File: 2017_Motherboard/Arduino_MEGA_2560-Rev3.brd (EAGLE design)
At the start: 100 x 80 mm, 77 parts, among them IC1 NCP1117ST50T3G, IC2 FT232RL, IC3 ATMEGA2560-16AU, IC7 LMV358IDGKR, X1 POWERSUPPLY_DC21MMX, Y1 CSTCE16M0V53-R0 16MHZ

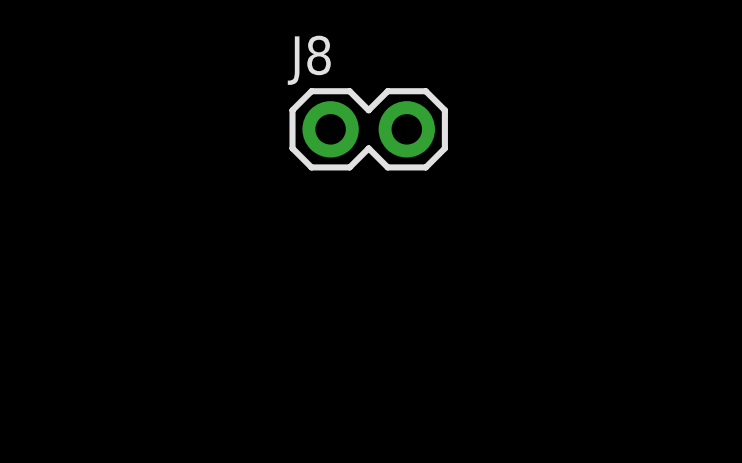
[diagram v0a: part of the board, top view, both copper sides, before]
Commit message: Added GND for PWMs
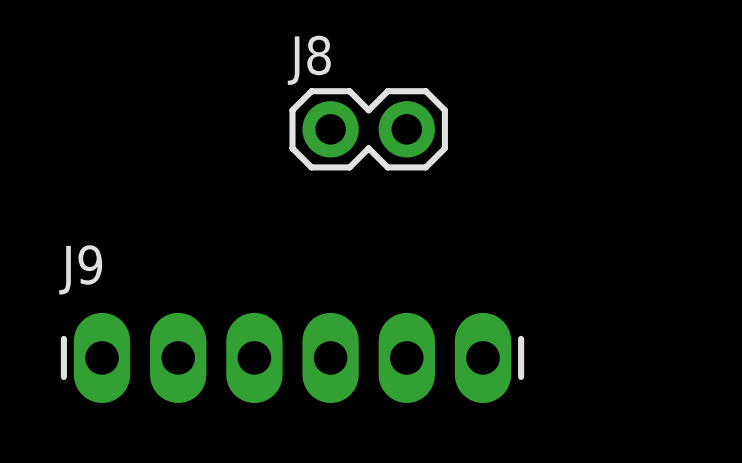
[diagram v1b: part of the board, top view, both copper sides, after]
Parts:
- added J9: (no value), SparkFun-Connectors:1X06_LONGPADS
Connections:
- net GND: now also J9.1, J9.2, J9.3, J9.4, J9.5, J9.6
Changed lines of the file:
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@@
 <?xml version="1.0" encoding="utf-8"?>
 <!DOCTYPE eagle SYSTEM "eagle.dtd">
-<eagle version="7.7.0">
+<eagle version="7.6.0">
 <drawing>
 <settings>
@@
 <element name="J7" library="SparkFun-Connectors" package="1X02" value="" x="-7.62" y="-266.7"/>
 <element name="J8" library="SparkFun-Connectors" package="1X02" value="" x="-7.62" y="-287.02"/>
+<element name="J9" library="SparkFun-Connectors" package="1X06_LONGPADS" value="" x="-15.24" y="-294.64"/>
 </elements>
 <signals>
@@
 <contactref element="J2" pad="4"/>
 <contactref element="J2" pad="3"/>
+<contactref element="J9" pad="6"/>
+<contactref element="J9" pad="5"/>
+<contactref element="J9" pad="4"/>
+<contactref element="J9" pad="3"/>
+<contactref element="J9" pad="2"/>
+<contactref element="J9" pad="1"/>
 <wire x1="-16.09" y1="-223.52" x2="-16.09" y2="-233.68" width="0" layer="19" extent="1-1"/>
 <wire x1="-8.47" y1="-223.52" x2="-16.09" y2="-223.52" width="0" layer="19" extent="1-1"/>
@@
 <wire x1="-16.09" y1="-86.36" x2="-16.09" y2="-91.44" width="0" layer="19" extent="1-1"/>
 <wire x1="-16.09" y1="-81.28" x2="-16.09" y2="-86.36" width="0" layer="19" extent="1-1"/>
+<wire x1="-15.24" y1="-294.64" x2="-16.09" y2="-233.68" width="0" layer="19" extent="1-1"/>
+<wire x1="-12.7" y1="-294.64" x2="-15.24" y2="-294.64" width="0" layer="19" extent="1-1"/>
+<wire x1="-10.16" y1="-294.64" x2="-12.7" y2="-294.64" width="0" layer="19" extent="1-1"/>
+<wire x1="-7.62" y1="-294.64" x2="-10.16" y2="-294.64" width="0" layer="19" extent="1-1"/>
+<wire x1="-5.08" y1="-294.64" x2="-7.62" y2="-294.64" width="0" layer="19" extent="1-1"/>
+<wire x1="-2.54" y1="-294.64" x2="-5.08" y2="-294.64" width="0" layer="19" extent="1-1"/>
 <wire x1="22.82" y1="2.46" x2="-16.09" y2="-81.28" width="0" layer="19" extent="1-1"/>
 <wire x1="25.36" y1="2.46" x2="22.82" y2="2.46" width="0" layer="19" extent="1-1"/>

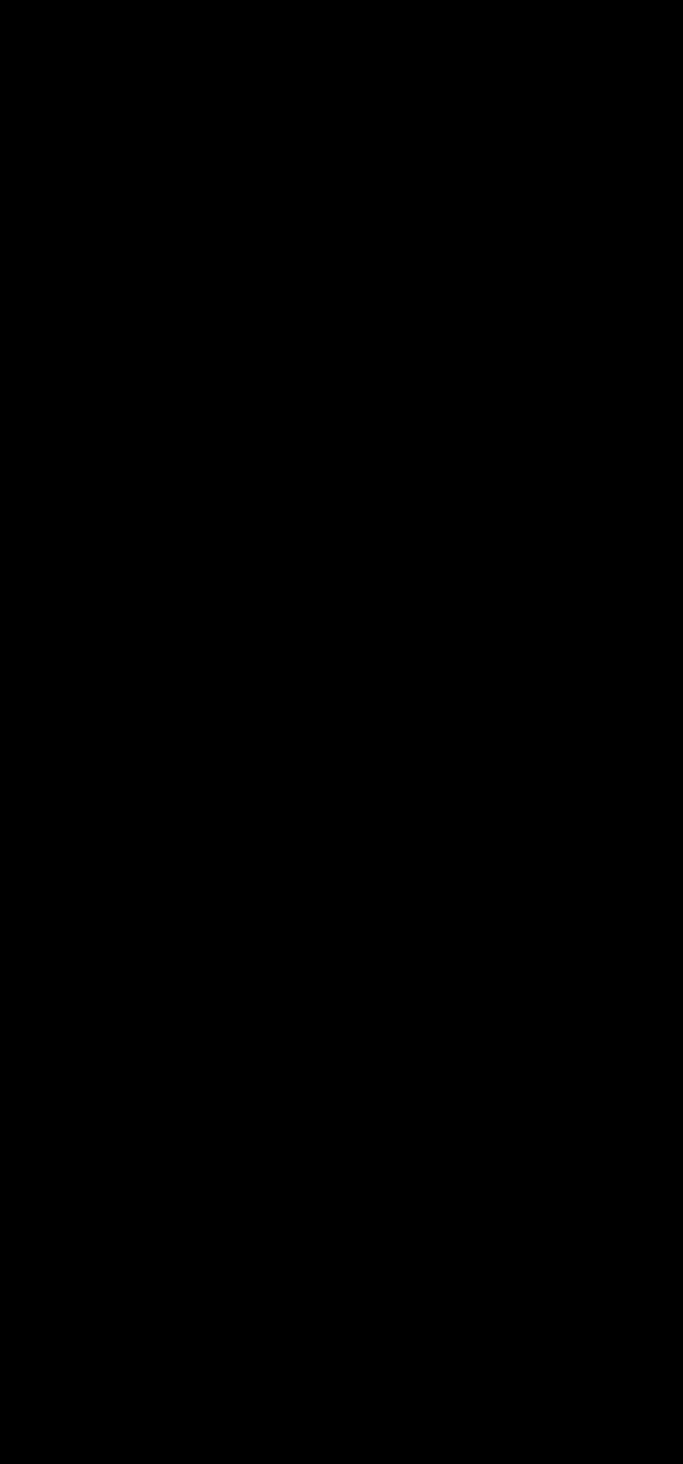
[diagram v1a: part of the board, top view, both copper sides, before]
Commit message: SchematicRev1
finished the schematic (hopefully), now we will work on the layout
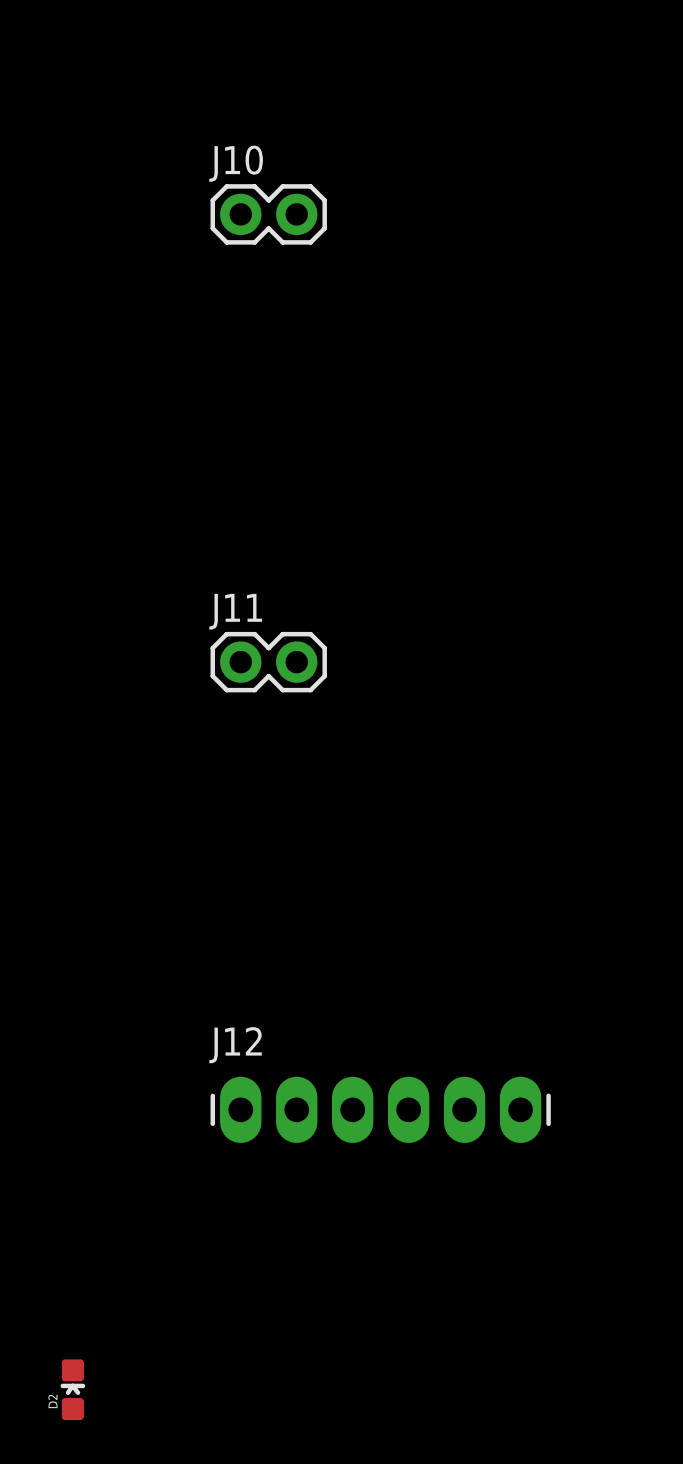
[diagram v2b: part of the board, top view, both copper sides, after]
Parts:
- added D2: RED, SparkFun-LED:LED-0603
- added J10, J11: (no value), SparkFun-Connectors:1X02
- added J12: (no value), SparkFun-Connectors:1X06_LONGPADS
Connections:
- new net N$15: D2.C, J11.2
- net +3V3: now also J10.1
- net +5V: now also J11.1, J12.2
- net FTDI_3.3V: now also J10.2
- net GND: now also J12.3
- net PA1: now also J12.6
- net PA2: now also J12.1
- net RXD1: now also J12.4
- net TXD1: now also J12.5
- net V_USB: now also D2.A
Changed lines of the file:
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@@
 <?xml version="1.0" encoding="utf-8"?>
 <!DOCTYPE eagle SYSTEM "eagle.dtd">
-<eagle version="7.6.0">
+<eagle version="7.7.0">
 <drawing>
 <settings>
@@
 <element name="J8" library="SparkFun-Connectors" package="1X02" value="" x="-7.62" y="-287.02"/>
 <element name="J9" library="SparkFun-Connectors" package="1X06_LONGPADS" value="" x="-15.24" y="-294.64"/>
+<element name="J10" library="SparkFun-Connectors" package="1X02" value="" x="-15.24" y="-314.96"/>
+<element name="J11" library="SparkFun-Connectors" package="1X02" value="" x="-15.24" y="-335.28"/>
+<element name="J12" library="SparkFun-Connectors" package="1X06_LONGPADS" value="" x="-15.24" y="-355.6"/>
+<element name="D2" library="SparkFun-LED" package="LED-0603" value="RED" x="-22.86" y="-368.3">
+<attribute name="PROD_ID" value="DIO-00819" x="-22.86" y="-368.3" size="1.778" layer="27" display="off"/>
+</element>
 </elements>
 <signals>
@@
 <contactref element="POWER" pad="5"/>
 <contactref element="POWER" pad="2"/>
+<contactref element="J11" pad="1"/>
+<contactref element="J12" pad="2"/>
 <wire x1="84.32" y1="67.43" x2="84.32" y2="68.23" width="0" layer="19" extent="1-1"/>
 <wire x1="84.98" y1="61.8" x2="84.32" y2="67.43" width="0" layer="19" extent="1-1"/>
@@
 <wire x1="18.74" y1="23.31" x2="16.7348" y2="12.78" width="0" layer="19" extent="1-1"/>
 <wire x1="36.265" y1="51.57" x2="54.8" y2="44.3464" width="0" layer="19" extent="1-1"/>
+<wire x1="-15.24" y1="-335.28" x2="27.9" y2="2.46" width="0" layer="19" extent="1-1"/>
+<wire x1="-12.7" y1="-355.6" x2="-15.24" y2="-335.28" width="0" layer="19" extent="1-1"/>
 </signal>
 <signal name="GND" class="2">
@@
 <contactref element="J9" pad="2"/>
 <contactref element="J9" pad="1"/>
+<contactref element="J12" pad="3"/>
 <wire x1="-16.09" y1="-223.52" x2="-16.09" y2="-233.68" width="0" layer="19" extent="1-1"/>
 <wire x1="-8.47" y1="-223.52" x2="-16.09" y2="-223.52" width="0" layer="19" extent="1-1"/>
@@
 <wire x1="-5.08" y1="-294.64" x2="-7.62" y2="-294.64" width="0" layer="19" extent="1-1"/>
 <wire x1="-2.54" y1="-294.64" x2="-5.08" y2="-294.64" width="0" layer="19" extent="1-1"/>
+<wire x1="-10.16" y1="-355.6" x2="-10.16" y2="-294.64" width="0" layer="19" extent="1-1"/>
 <wire x1="22.82" y1="2.46" x2="-16.09" y2="-81.28" width="0" layer="19" extent="1-1"/>
 <wire x1="25.36" y1="2.46" x2="22.82" y2="2.46" width="0" layer="19" extent="1-1"/>
@@
 <contactref element="POWER" pad="4"/>
 <contactref element="J8" pad="1"/>
+<contactref element="J10" pad="1"/>
+<wire x1="-7.62" y1="-287.02" x2="-15.24" y2="-314.96" width="0" layer="19" extent="1-1"/>
 <wire x1="30.44" y1="2.46" x2="-7.62" y2="-287.02" width="0" layer="19" extent="1-1"/>
 </signal>
@@
 <contactref element="IC3" pad="45"/>
 <contactref element="COMMUNICATION" pad="3"/>
+<contactref element="J12" pad="4"/>
 <wire x1="64.3" y1="28.3464" x2="79.28" y2="75.8" width="0" layer="19" extent="1-1"/>
+<wire x1="-7.62" y1="-355.6" x2="64.3" y2="28.3464" width="0" layer="19" extent="1-1"/>
 </signal>
 <signal name="TXD1">
 <contactref element="IC3" pad="46"/>
 <contactref element="COMMUNICATION" pad="4"/>
+<contactref element="J12" pad="5"/>
 <wire x1="64.8" y1="28.3464" x2="76.74" y2="75.8" width="0" layer="19" extent="1-1"/>
+<wire x1="-5.08" y1="-355.6" x2="64.8" y2="28.3464" width="0" layer="19" extent="1-1"/>
 </signal>
 <signal name="RXD2">
@@
 <contactref element="IC3" pad="77"/>
 <contactref element="XIO" pad="4"/>
+<contactref element="J12" pad="6"/>
 <wire x1="66.3" y1="44.3464" x2="87.52" y2="59.26" width="0" layer="19" extent="1-1"/>
+<wire x1="-2.54" y1="-355.6" x2="66.3" y2="44.3464" width="0" layer="19" extent="1-1"/>
 </signal>
 <signal name="PA2">
 <contactref element="IC3" pad="76"/>
 <contactref element="XIO" pad="5"/>
+<contactref element="J12" pad="1"/>
 <wire x1="66.8" y1="44.3464" x2="84.98" y2="56.72" width="0" layer="19" extent="1-1"/>
+<wire x1="-15.24" y1="-355.6" x2="66.8" y2="44.3464" width="0" layer="19" extent="1-1"/>
 </signal>
 <signal name="PA3">
@@
 <contactref element="C17" pad="1"/>
 <contactref element="R21" pad="2"/>
+<contactref element="J10" pad="2"/>
 <wire x1="-0.85" y1="-213.36" x2="0.85" y2="-223.52" width="0" layer="19" extent="1-1"/>
 <wire x1="2.925" y1="-197.035" x2="-0.85" y2="-213.36" width="0" layer="19" extent="1-1"/>
+<wire x1="-12.7" y1="-314.96" x2="0.85" y2="-223.52" width="0" layer="19" extent="1-1"/>
 </signal>
 <signal name="V_USB">
@@
 <contactref element="C19" pad="1"/>
 <contactref element="C18" pad="1"/>
+<contactref element="D2" pad="A"/>
 <wire x1="-16.09" y1="-213.36" x2="-16.09" y2="-218.44" width="0" layer="19" extent="1-1"/>
 <wire x1="-8.47" y1="-218.44" x2="-16.09" y2="-218.44" width="0" layer="19" extent="1-1"/>
@@
 <wire x1="0.975" y1="-197.035" x2="-2.275" y2="-204.285" width="0" layer="19" extent="1-1"/>
 <wire x1="-9.975" y1="-201.9" x2="-2.275" y2="-204.285" width="0" layer="19" extent="1-1"/>
+<wire x1="-22.86" y1="-369.177" x2="-16.09" y2="-218.44" width="0" layer="19" extent="1-1"/>
 </signal>
 <signal name="RESET_B">
@@
 <wire x1="2.76" y1="59.85" x2="-5.08" y2="-246.38" width="0" layer="19" extent="1-1"/>
 </signal>
+<signal name="N$15">
+<contactref element="J11" pad="2"/>
+<contactref element="D2" pad="C"/>
+<wire x1="-12.7" y1="-335.28" x2="-22.86" y2="-367.423" width="0" layer="19" extent="1-1"/>
+</signal>
 </signals>

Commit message: switched led on USB line to parallel
LED will now not drop the voltage
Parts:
- removed RN1, RN5: 10K, resistor-dil:CAT16
- removed RN3: 1k, resistor-dil:CAY16
- added J13: (no value), SparkFun-Connectors:1X04_LONGPADS
- added R25, R26, R27: 10K, SparkFun-Resistors:0603-RES
- added R28, R29, R30: 1K, SparkFun-Resistors:0603-RES
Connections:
- new net N$16: JP6.2
- net +5V: now also R25.2, R26.2, R27.2, R28.1; no longer RN1.6, RN1.7, RN3.1, RN5.8
- net GND: now also J13.3, J13.4, R30.1
- net L13: now also R29.1; no longer RN3.7
- net N$15: now also R30.2; no longer J11.2
- net N$2: now also R29.2; no longer RN3.2
- net N$3: now also R28.2; no longer RN3.8
- net RESET: now also R27.1; no longer RN5.1
- net RXD2: now also J13.2
- net SCL: now also R26.1; no longer RN1.2
- net SDA: now also R25.1; no longer JP6.2, RN1.3
- net TXD2: now also J13.1
- net V_USB: now also J11.2

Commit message: Video Out Laid out
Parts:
- added IC4: MAX4312ESE, maxim:SO16
- added IC5: MAX3468CPA, maxim:DIL08
- added RXD2_JUMPER, TXD2_JUMPER: (no value), SparkFun-Connectors:1X02
- added VIDEO_IN, VIDEO_IN_GND: 8x1F-H8.5, SmartPrj:1X08
- added VIDEO_OUT: A1944-50, con-coax:A1944
- moved R30 436.7 mm to (2.29, 37.3), turned to 180 degrees
- moved D2 408.4 mm to (2.29, 39.4), turned to 90 degrees
- moved J11 375.8 mm to (10.2, 39.6), turned to 90 degrees
- moved J10 368.8 mm to (3.05, 53.3)
- moved R19 281.5 mm to (24.9, 55.1), turned to 180 degrees
- moved R21 281.4 mm to (19.6, 57.1), turned to 180 degrees
- moved R24 278.6 mm to (16.0, 43.2)
- moved R18 273.2 mm to (24.9, 53.6), turned to 180 degrees
- moved R23 271.3 mm to (16.0, 41.7), turned to 180 degrees
- moved C17 270.9 mm to (15.2, 57.1)
- moved R22 270.3 mm to (16.0, 39.9)
- moved R20 269.3 mm to (16.0, 44.7)
- moved C18 265.8 mm to (11.9, 46.0), turned to 270 degrees
- moved C19 265.0 mm to (10.4, 46.0), turned to 270 degrees
- moved IC2 252.1 mm to (17.8, 50.8), turned to 90 degrees
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- renumbered J12 to BLUETOOTH_J6, J9 to ESC_PWM_GND
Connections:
- removed net RESET_B: R22.1
- new net RXD2_OUT: IC5.6, J13.2, RXD2_JUMPER.2
- new net S$2: IC4.13, IC4.14, IC4.15
- new net TXD2_OUT: IC5.7, J13.1, TXD2_JUMPER.2
- new net VIDEO_OUT: IC4.16, VIDEO_OUT.1
- new net VID_0: IC4.5, VIDEO_IN.1
- new net VID_1: IC4.6, VIDEO_IN.2
- new net VID_2: IC4.7, VIDEO_IN.3
- new net VID_3: IC4.8, VIDEO_IN.4
- new net VID_4: IC4.9, VIDEO_IN.5
- new net VID_5: IC4.10, VIDEO_IN.6
- new net VID_6: IC4.11, VIDEO_IN.7
- new net VID_7: IC4.12, VIDEO_IN.8
- net +5V: now also IC4.4, IC5.8
- net GND: now also IC5.5, VIDEO_IN_GND.1, VIDEO_IN_GND.2, VIDEO_IN_GND.3, VIDEO_IN_GND.4, VIDEO_IN_GND.5, VIDEO_IN_GND.6, VIDEO_IN_GND.7, VIDEO_IN_GND.8, VIDEO_OUT.2, VIDEO_OUT.3, VIDEO_OUT.4, VIDEO_OUT.5
- net PA3: now also IC4.3
- net PA4: now also IC4.2
- net PA5: now also IC4.1
- net PA6: now also IC5.2
- net PA7: now also IC5.3
- net RESET: now also R22.1
- net RXD2: now also IC5.1, RXD2_JUMPER.1; no longer J13.2
- net TXD2: now also IC5.4, TXD2_JUMPER.1; no longer J13.1
- net V_USB: now also R23.2
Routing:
- net V_USB: track 0.00 -> 47.3 mm, vias 0 -> 2
- net GND: track 0.00 -> 30.5 mm, vias 0 -> 7
- net PA3: track 0.00 -> 29.3 mm, vias 0 -> 2
- net PA4: track 0.00 -> 24.7 mm, vias 0 -> 2
- net PA5: track 0.00 -> 20.6 mm
- net FTDI_3.3V: track 0.00 -> 20.2 mm
- net N$4: track 0.00 -> 18.2 mm, vias 0 -> 2
- net VIDEO_OUT: track 0.00 -> 16.8 mm
- net USBDP: track 0.00 -> 16.5 mm, vias 0 -> 2
- net USBDN: track 0.00 -> 15.6 mm
- net VID_7: track 0.00 -> 15.2 mm
- net VID_0: track 0.00 -> 14.9 mm
- net VID_1: track 0.00 -> 11.9 mm
- net VID_6: track 0.00 -> 11.9 mm
- net FTDI_CBUS1: track 0.00 -> 11.6 mm
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- added copper zone on layer 1, net +3V3
- added copper zone on layer 1, net +5V
- added copper zone on layer 16, net GND
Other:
- board text added: "Aground on the FTDI is not connected to anything at the moment"

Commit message: Revert "Video Out Laid out", schematic lost video
This reverts commit bce98d3cfb039a053e1cc747be892bf7f1308c0a.
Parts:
- removed IC4: MAX4312ESE, maxim:SO16
- removed IC5: MAX3468CPA, maxim:DIL08
- removed RXD2_JUMPER, TXD2_JUMPER: (no value), SparkFun-Connectors:1X02
- removed VIDEO_IN, VIDEO_IN_GND: 8x1F-H8.5, SmartPrj:1X08
- removed VIDEO_OUT: A1944-50, con-coax:A1944
- moved R30 436.7 mm to (-20.3, -398.8), turned to 0 degrees
- moved D2 408.4 mm to (-22.9, -368.3), turned to 0 degrees
- moved J11 375.8 mm to (-15.2, -335.3), turned to 0 degrees
- moved J10 368.8 mm to (-15.2, -315.0)
- moved R19 281.5 mm to (-15.2, -223.5), turned to 0 degrees
- moved R21 281.4 mm to (0.00, -223.5), turned to 0 degrees
- moved R24 278.6 mm to (-15.2, -233.7)
- moved R18 273.2 mm to (0.00, -218.4), turned to 0 degrees
- moved R23 271.3 mm to (-7.62, -228.6), turned to 0 degrees
- moved C17 270.9 mm to (0.00, -213.4)
- moved R22 270.3 mm to (-15.2, -228.6)
- moved R20 269.3 mm to (-7.62, -223.5)
- moved C18 265.8 mm to (-15.2, -218.4), turned to 0 degrees
- moved C19 265.0 mm to (-7.62, -218.4), turned to 0 degrees
- moved IC2 252.1 mm to (0.00, -200.7), turned to 0 degrees
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- renumbered BLUETOOTH_J6 to J12, ESC_PWM_GND to J9
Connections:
- removed net RXD2_OUT: IC5.6, J13.2, RXD2_JUMPER.2
- removed net S$2: IC4.13, IC4.14, IC4.15
- removed net TXD2_OUT: IC5.7, J13.1, TXD2_JUMPER.2
- removed net VIDEO_OUT: IC4.16, VIDEO_OUT.1
- removed net VID_0: IC4.5, VIDEO_IN.1
- removed net VID_1: IC4.6, VIDEO_IN.2
- removed net VID_2: IC4.7, VIDEO_IN.3
- removed net VID_3: IC4.8, VIDEO_IN.4
- removed net VID_4: IC4.9, VIDEO_IN.5
- removed net VID_5: IC4.10, VIDEO_IN.6
- removed net VID_6: IC4.11, VIDEO_IN.7
- removed net VID_7: IC4.12, VIDEO_IN.8
- new net RESET_B: R22.1
- net +5V: no longer IC4.4, IC5.8
- net GND: no longer IC5.5, VIDEO_IN_GND.1, VIDEO_IN_GND.2, VIDEO_IN_GND.3, VIDEO_IN_GND.4, VIDEO_IN_GND.5, VIDEO_IN_GND.6, VIDEO_IN_GND.7, VIDEO_IN_GND.8, VIDEO_OUT.2, VIDEO_OUT.3, VIDEO_OUT.4, VIDEO_OUT.5
- net PA3: no longer IC4.3
- net PA4: no longer IC4.2
- net PA5: no longer IC4.1
- net PA6: no longer IC5.2
- net PA7: no longer IC5.3
- net RESET: no longer R22.1
- net RXD2: now also J13.2; no longer IC5.1, RXD2_JUMPER.1
- net TXD2: now also J13.1; no longer IC5.4, TXD2_JUMPER.1
- net V_USB: no longer R23.2
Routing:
- net V_USB: track 47.3 -> 0.00 mm, vias 2 -> 0
- net GND: track 30.5 -> 0.00 mm, vias 7 -> 0
- net PA3: track 29.3 -> 0.00 mm, vias 2 -> 0
- net PA4: track 24.7 -> 0.00 mm, vias 2 -> 0
- net PA5: track 20.6 -> 0.00 mm
- net FTDI_3.3V: track 20.2 -> 0.00 mm
- net N$4: track 18.2 -> 0.00 mm, vias 2 -> 0
- net VIDEO_OUT: track 16.8 -> 0.00 mm
- net USBDP: track 16.5 -> 0.00 mm, vias 2 -> 0
- net USBDN: track 15.6 -> 0.00 mm
- net VID_7: track 15.2 -> 0.00 mm
- net VID_0: track 14.9 -> 0.00 mm
- net VID_1: track 11.9 -> 0.00 mm
- net VID_6: track 11.9 -> 0.00 mm
- net FTDI_CBUS1: track 11.6 -> 0.00 mm
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- removed copper zone on layer 1, net +3V3
- removed copper zone on layer 1, net +5V
- removed copper zone on layer 16, net GND
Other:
- board text removed: "Aground on the FTDI is not connected to anything at the moment"
